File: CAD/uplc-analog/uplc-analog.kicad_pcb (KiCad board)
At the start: 4 copper layers, 31.4 x 21 mm, 69 parts, among them J1 Conn_01x06_Pin, J2 SM12B-GHS-TB(LF)(SN), U1 AP63201WU, U2 ADS1115IDGS, U3 ESP32-C3-WROOM-02, U4 LP5907MFX-3.0, U5 MCP4725xxx-xCH, Y1 32.768khz 3215 12.5pf

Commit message: Rev 1.1
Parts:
- removed kibuzzard-65DC9C3C: G***, kibuzzard-65DC9C3C
- added kibuzzard-65DCE4DE: G***, kibuzzard-65DCE4DE, F.Cu at (104.5, 82.6)
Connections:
- U3 pad 10: unconnected-(U3-GPIO10-Pad10) -> ADC_DRDY
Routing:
- net ADC_DRDY: track 2.73 -> 17.9 mm, vias 0 -> 1
- net GND: track 41.2 -> 42.8 mm, vias 70 -> 72
- net +3.3V: track 104.4 -> 105.2 mm
- net +3V0: track 32.0 -> 32.5 mm

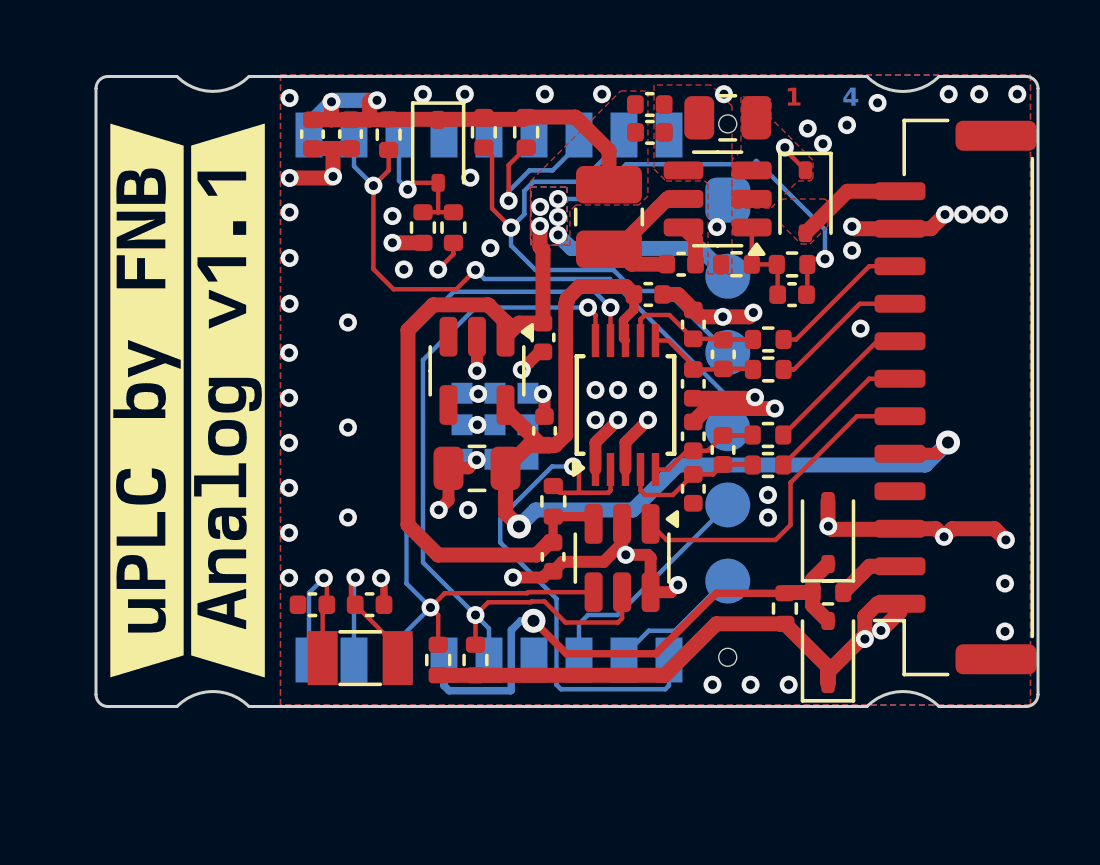
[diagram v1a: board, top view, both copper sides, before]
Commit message: Panelization changes
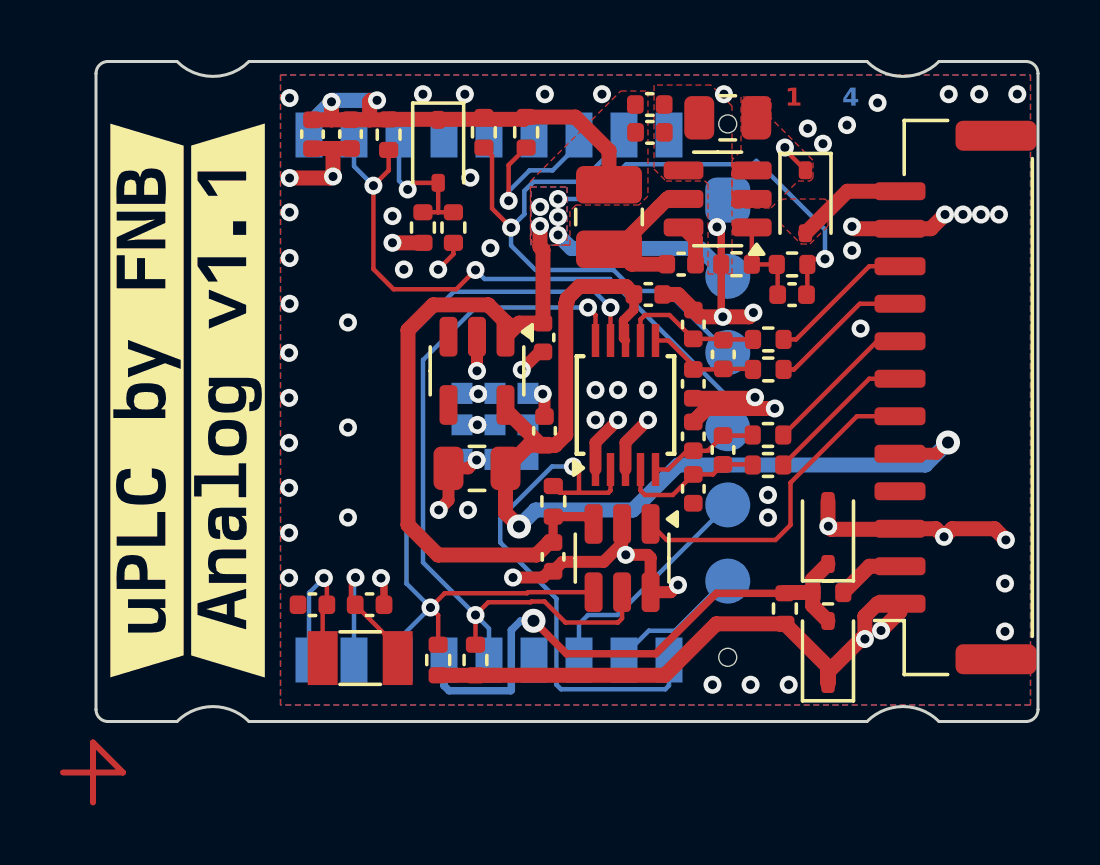
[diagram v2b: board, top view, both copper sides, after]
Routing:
- net GND: track 42.8 -> 45.9 mm
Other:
- board size 31.4 x 21 mm -> 31.4 x 22 mm

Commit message: Updated readme and documentation to analog
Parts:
- removed kibuzzard-65D8B121: G***, kibuzzard-65D8B121
- added kibuzzard-65D74DE1: G***, kibuzzard-65D74DE1, B.Cu at (128.4, 86.4)
- moved kibuzzard-65DC961D 1.55 mm to (128.4, 84.9)

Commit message: feat: Production update
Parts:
- C19, C20: value 1uF -> 0.1uF
- L1: value 6.8uH -> 4.7uH
